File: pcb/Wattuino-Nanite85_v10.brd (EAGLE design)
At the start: 17.5 x 10.2 mm, 18 parts, among them IC2 ATTINY85-MU, J1 USB-MICRO, J2 MA04-1, J3 MA04-1, SW1 SW-TACTILE-PTS840P, X1 PASSER-07, X2 PASSER-07, X3 PASSER-07

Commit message: updated Tiny85/Nanite85
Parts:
- D1, D2: value uClamp2511T -> Z3V6
- R4: value 2k2 -> 1k5
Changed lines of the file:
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@@
 <attribute name="NAME" x="10.0203" y="4.60375" size="0.8128" layer="25" font="vector" ratio="10" align="center"/>
 </element>
-<element name="R4" library="we-rcl" package="R0402" value="2k2" x="8.1153" y="6.50875" smashed="yes" rot="R270">
+<element name="R4" library="we-rcl" package="R0402" value="1k5" x="8.1153" y="6.50875" smashed="yes" rot="R270">
 <attribute name="NAME" x="10.0203" y="6.50875" size="0.8128" layer="25" font="vector" ratio="10" align="center"/>
 </element>
@@
 <attribute name="NAME" x="6.3246" y="0.635" size="0.8128" layer="25" font="vector" ratio="10" align="center"/>
 </element>
-<element name="D2" library="we-rcl" package="SOD882" value="uClamp2511T" x="6.19125" y="6.0325" smashed="yes" rot="R180">
+<element name="D2" library="we-rcl" package="SOD882" value="Z3V6" x="6.19125" y="6.0325" smashed="yes" rot="R180">
 <attribute name="NAME" x="7.3025" y="5.55625" size="0.8128" layer="25" font="vector" ratio="10" rot="R180" align="center"/>
 </element>
-<element name="D1" library="we-rcl" package="SOD882" value="uClamp2511T" x="6.19125" y="4.1275" smashed="yes">
+<element name="D1" library="we-rcl" package="SOD882" value="Z3V6" x="6.19125" y="4.1275" smashed="yes">
 <attribute name="NAME" x="7.3025" y="4.1275" size="0.8128" layer="25" font="vector" ratio="10" align="center"/>
 </element>

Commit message: updated layout and schematics
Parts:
- C1, R1, R2, R3, R4: device we-rcl:R0402 -> we-rcl:C0402

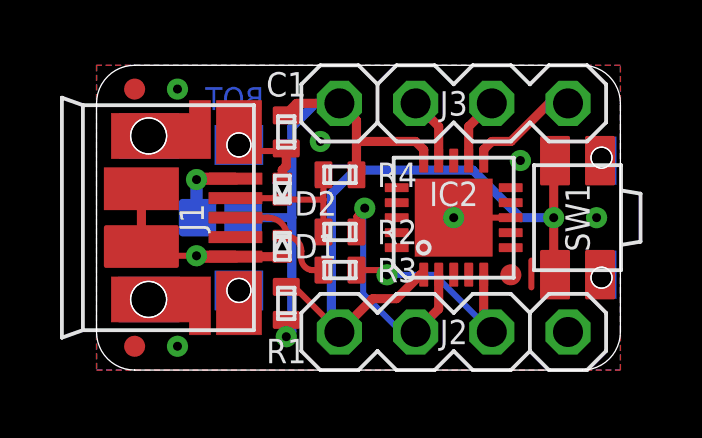
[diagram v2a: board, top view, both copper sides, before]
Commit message: updated schematics
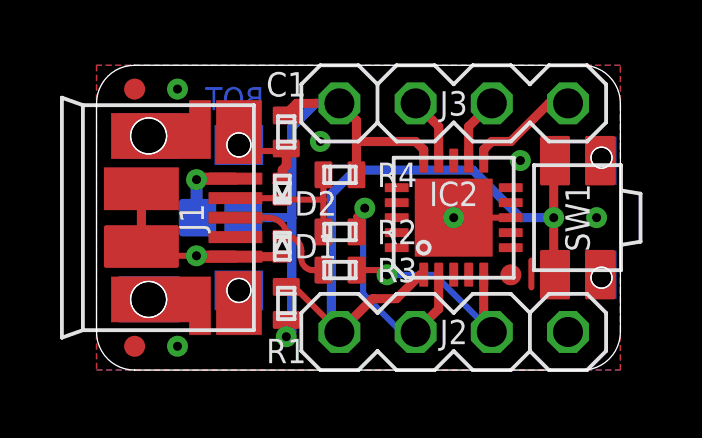
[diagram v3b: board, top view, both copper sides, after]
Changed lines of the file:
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@@
 <layer number="48" name="Document" color="7" fill="1" visible="yes" active="yes"/>
 <layer number="49" name="Reference" color="7" fill="1" visible="yes" active="yes"/>
+<layer number="50" name="dxf" color="7" fill="1" visible="no" active="no"/>
 <layer number="51" name="tDocu" color="7" fill="1" visible="yes" active="yes"/>
 <layer number="52" name="bDocu" color="7" fill="1" visible="yes" active="yes"/>
@@
 </class>
 </classes>
-<designrules name="default *">
-<description language="de">&lt;b&gt;EAGLE Design Rules&lt;/b&gt;
-&lt;p&gt;
-Die Standard-Design-Rules sind so gewählt, dass sie für
-die meisten Anwendungen passen. Sollte ihre Platine
-besondere Anforderungen haben, treffen Sie die erforderlichen
-Einstellungen hier und speichern die Design Rules unter
-einem neuen Namen ab.</description>
-<description language="en">&lt;b&gt;EAGLE Design Rules&lt;/b&gt;
-&lt;p&gt;
-The default Design Rules have been set to cover
-a wide range of applications. Your particular design
-may have different requirements, so please make the
-necessary adjustments and save your customized
-design rules under a new name.</description>
+<designrules name="we-dru *">
+<description language="de">&lt;b&gt;PCB Design Rules&lt;/b&gt;</description>
+<description language="en">&lt;b&gt;PCB Design Rules&lt;/b&gt;</description>
 <param name="layerSetup" value="(1*16)"/>
 <param name="mtCopper" value="0.035mm 0.035mm 0.035mm 0.035mm 0.035mm 0.035mm 0.035mm 0.035mm 0.035mm 0.035mm 0.035mm 0.035mm 0.035mm 0.035mm 0.035mm 0.035mm"/>
 <param name="mtIsolate" value="1.5mm 0.15mm 0.2mm 0.15mm 0.2mm 0.15mm 0.2mm 0.15mm 0.2mm 0.15mm 0.2mm 0.15mm 0.2mm 0.15mm 0.2mm"/>
-<param name="mdWireWire" value="7mil"/>
-<param name="mdWirePad" value="7mil"/>
-<param name="mdWireVia" value="7mil"/>
-<param name="mdPadPad" value="7mil"/>
-<param name="mdPadVia" value="7mil"/>
-<param name="mdViaVia" value="7mil"/>
-<param name="mdSmdPad" value="7mil"/>
-<param name="mdSmdVia" value="7mil"/>
-<param name="mdSmdSmd" value="7mil"/>
-<param name="mdViaViaSameLayer" value="8mil"/>
+<param name="mdWireWire" value="0.15mm"/>
+<param name="mdWirePad" value="0.15mm"/>
+<param name="mdWireVia" value="0.15mm"/>
+<param name="mdPadPad" value="0.15mm"/>
+<param name="mdPadVia" value="0.15mm"/>
+<param name="mdViaVia" value="0.15mm"/>
+<param name="mdSmdPad" value="0.1mm"/>
+<param name="mdSmdVia" value="0.1mm"/>
+<param name="mdSmdSmd" value="0.1mm"/>
+<param name="mdViaViaSameLayer" value="0.2mm"/>
 <param name="mnLayersViaInSmd" value="2"/>
 <param name="mdCopperDimension" value="0.3mm"/>
-<param name="mdDrill" value="8mil"/>
+<param name="mdDrill" value="0.2mm"/>
 <param name="mdSmdStop" value="0mil"/>
-<param name="msWidth" value="8mil"/>
+<param name="msWidth" value="0.15mm"/>
 <param name="msDrill" value="0.3mm"/>
 <param name="msMicroVia" value="9.99mm"/>
 <param name="msBlindViaRatio" value="0.5"/>
-<param name="rvPadTop" value="0.25"/>
-<param name="rvPadInner" value="0.25"/>
-<param name="rvPadBottom" value="0.25"/>
+<param name="rvPadTop" value="0.2"/>
+<param name="rvPadInner" value="0.2"/>
+<param name="rvPadBottom" value="0.2"/>
 <param name="rvViaOuter" value="0.25"/>
 <param name="rvViaInner" value="0.25"/>
 <param name="rvMicroViaOuter" value="0.25"/>
 <param name="rvMicroViaInner" value="0.25"/>
-<param name="rlMinPadTop" value="10mil"/>
-<param name="rlMaxPadTop" value="20mil"/>
-<param name="rlMinPadInner" value="10mil"/>
-<param name="rlMaxPadInner" value="20mil"/>
-<param name="rlMinPadBottom" value="10mil"/>
-<param name="rlMaxPadBottom" value="20mil"/>
-<param name="rlMinViaOuter" value="8mil"/>
-<param name="rlMaxViaOuter" value="20mil"/>
-<param name="rlMinViaInner" value="8mil"/>
-<param name="rlMaxViaInner" value="20mil"/>
-<param name="rlMinMicroViaOuter" value="4mil"/>
-<param name="rlMaxMicroViaOuter" value="20mil"/>
-<param name="rlMinMicroViaInner" value="4mil"/>
-<param name="rlMaxMicroViaInner" value="20mil"/>
+<param name="rlMinPadTop" value="0.18mm"/>
+<param name="rlMaxPadTop" value="0.5mm"/>
+<param name="rlMinPadInner" value="0.18mm"/>
+<param name="rlMaxPadInner" value="0.5mm"/>
+<param name="rlMinPadBottom" value="0.18mm"/>
+<param name="rlMaxPadBottom" value="0.5mm"/>
+<param name="rlMinViaOuter" value="0.2mm"/>
+<param name="rlMaxViaOuter" value="0.5mm"/>
+<param name="rlMinViaInner" value="0.2mm"/>
+<param name="rlMaxViaInner" value="0.5mm"/>
+<param name="rlMinMicroViaOuter" value="0.1mm"/>
+<param name="rlMaxMicroViaOuter" value="0.5mm"/>
+<param name="rlMinMicroViaInner" value="0.1mm"/>
+<param name="rlMaxMicroViaInner" value="0.5mm"/>
 <param name="psTop" value="-1"/>
 <param name="psBottom" value="-1"/>
@@
 <param name="mvStopFrame" value="1"/>
 <param name="mvCreamFrame" value="0"/>
-<param name="mlMinStopFrame" value="0.3mm"/>
-<param name="mlMaxStopFrame" value="4mil"/>
+<param name="mlMinStopFrame" value="0.1mm"/>
+<param name="mlMaxStopFrame" value="0.1mm"/>
 <param name="mlMinCreamFrame" value="0mil"/>
 <param name="mlMaxCreamFrame" value="0mil"/>
@@
 <param name="srMinRoundness" value="0mil"/>
 <param name="srMaxRoundness" value="0mil"/>
-<param name="slThermalIsolate" value="8mil"/>
+<param name="slThermalIsolate" value="0.25mm"/>
 <param name="slThermalsForVias" value="0"/>
-<param name="dpMaxLengthDifference" value="2mm"/>
+<param name="dpMaxLengthDifference" value="5mm"/>
 <param name="dpGapFactor" value="2.5"/>
 <param name="checkGrid" value="0"/>
